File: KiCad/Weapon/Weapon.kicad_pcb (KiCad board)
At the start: 2 copper layers, 97.3 x 74.4 mm, 33 parts, among them IC1 ATMEGA328-P, J1 MICRO_USB, P1 2P_CGRID_M, P2 USB-TTL, P3 2P_CGRID_M, Q1 NPN, Q2 NPN, U1 MCP73831, U2 RFID-RC522, U3 LM1084IT-3.3/NOPB, X1 16MHz

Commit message: Quick Update #1 4/28
Added resistor (220) to buzzer in weapon sch,net,pcb
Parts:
- added R7: 220, R4, F.Cu at (53.9, 77.1)
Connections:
- LS1 pad 1: N-0000013 -> N-0000014
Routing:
- net N-0000013: track 15.8 -> 3.79 mm
- net N-0000014: track 0.00 -> 10.2 mm

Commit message: Quick Update #2 4/28
Changes to Weapon PCB
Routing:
- net GND: track 55.6 -> 2.55 mm
- net +3.3V: track 32.7 -> 0.00 mm
- net N-000001: track 14.2 -> 10.9 mm
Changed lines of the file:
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@@
     (links 66)
     (no_connects 0)
-    (area 32.207999 17.082299 129.590001 91.629701)
+    (area 32.002999 17.082299 129.590001 91.629701)
     (thickness 1.6)
     (drawings 28)
-    (tracks 177)
+    (tracks 168)
     (zones 0)
     (modules 34)
@@
   (gr_line (start 32.258 60.452) (end 70.358 60.452) (angle 90) (layer F.SilkS) (width 0.2))
   (gr_line (start 32.258 35.052) (end 32.258 60.452) (angle 90) (layer F.SilkS) (width 0.2))
-  (segment (start 87.4776 47.4218) (end 97.536 47.4218) (width 0.508) (layer B.Cu) (net 1))
-  (segment (start 100.3808 44.577) (end 100.3808 25.92832) (width 0.508) (layer B.Cu) (net 1))
-  (segment (start 97.536 47.4218) (end 100.3808 44.577) (width 0.508) (layer B.Cu) (net 1))
-  (segment (start 85.344 43.942) (end 87.44712 43.942) (width 0.508) (layer F.Cu) (net 2))
-  (segment (start 87.44712 43.942) (end 92.75826 38.63086) (width 0.508) (layer F.Cu) (net 2))
-  (segment (start 92.75826 38.63086) (end 105.4608 25.92832) (width 0.508) (layer F.Cu) (net 2))
-  (segment (start 87.44712 43.942) (end 105.4608 25.92832) (width 0.254) (layer F.Cu) (net 2))
   (segment (start 37.807 67.198) (end 39.6644 67.198) (width 0.391) (layer F.Cu) (net 2))
   (segment (start 39.6644 67.198) (end 40.1574 67.691) (width 0.391) (layer F.Cu) (net 2))
@@
   (segment (start 73.7235 80.137) (end 73.7235 79.9465) (width 0.254) (layer B.Cu) (net 4))
   (segment (start 73.7235 79.9465) (end 77.216 76.454) (width 0.254) (layer B.Cu) (net 4))
-  (segment (start 36.068 33.147) (end 36.068 27.432) (width 0.254) (layer B.Cu) (net 5))
-  (segment (start 36.322 27.178) (end 44.45 27.178) (width 0.254) (layer B.Cu) (net 5))
-  (segment (start 36.068 27.432) (end 36.322 27.178) (width 0.254) (layer B.Cu) (net 5))
+  (segment (start 44.45 27.178) (end 42.037 27.178) (width 0.508) (layer B.Cu) (net 5))
+  (segment (start 42.037 27.178) (end 36.068 33.147) (width 0.508) (layer B.Cu) (net 5))
   (segment (start 63.5635 80.137) (end 59.8805 80.137) (width 0.254) (layer B.Cu) (net 6))
   (segment (start 59.8805 80.137) (end 59.563 80.4545) (width 0.254) (layer B.Cu) (net 6))
-  (segment (start 57.023 80.4545) (end 55.6895 80.4545) (width 0.508) (layer B.Cu) (net 7) (status 400000))
-  (segment (start 55.6895 80.4545) (end 53.9496 82.1944) (width 0.508) (layer B.Cu) (net 7) (status 800000))
-  (segment (start 53.9496 72.0344) (end 56.5631 72.0344) (width 0.508) (layer B.Cu) (net 8) (status 400000))
-  (segment (start 56.5631 72.0344) (end 61.9125 66.685) (width 0.508) (layer B.Cu) (net 8) (status 800000))
+  (segment (start 57.023 80.4545) (end 55.6895 80.4545) (width 0.508) (layer B.Cu) (net 7))
+  (segment (start 55.6895 80.4545) (end 53.9496 82.1944) (width 0.508) (layer B.Cu) (net 7))
+  (segment (start 53.9496 72.0344) (end 56.5631 72.0344) (width 0.508) (layer B.Cu) (net 8))
+  (segment (start 56.5631 72.0344) (end 61.9125 66.685) (width 0.508) (layer B.Cu) (net 8))
   (segment (start 52.705 66.294) (end 52.705 64.262) (width 0.254) (layer B.Cu) (net 9))
   (segment (start 52.705 64.262) (end 54.864 62.103) (width 0.254) (layer B.Cu) (net 9))
@@
   (segment (start 71.882 50.038) (end 71.882 52.578) (width 0.254) (layer F.Cu) (net 26))
   (via (at 71.882 50.038) (size 0.889) (layers F.Cu B.Cu) (net 26))
+  (segment (start 45.0215 32.7152) (end 45.0215 31.7373) (width 0.508) (layer B.Cu) (net 27))
+  (segment (start 45.0215 31.7373) (end 47.2948 29.464) (width 0.508) (layer B.Cu) (net 27))
   (segment (start 71.5264 43.307) (end 68.6054 40.386) (width 0.508) (layer F.Cu) (net 27))
   (segment (start 73.533 43.307) (end 71.5264 43.307) (width 0.508) (layer F.Cu) (net 27))
@@
   (segment (start 82.042 40.894) (end 82.042 42.164) (width 0.508) (layer B.Cu) (net 27))
   (segment (start 82.042 42.164) (end 80.264 43.942) (width 0.508) (layer B.Cu) (net 27))
-  (segment (start 46.6725 29.464) (end 49.403 29.464) (width 0.508) (layer B.Cu) (net 27))
-  (segment (start 46.6725 29.464) (end 46.609 29.464) (width 0.254) (layer B.Cu) (net 27))
-  (segment (start 46.609 29.464) (end 46.609 31.496) (width 0.508) (layer B.Cu) (net 27))
-  (segment (start 46.609 31.496) (end 46.482 31.623) (width 0.254) (layer B.Cu) (net 27))
-  (segment (start 46.482 31.623) (end 45.0215 31.623) (width 0.508) (layer B.Cu) (net 27))
-  (segment (start 45.0215 31.623) (end 45.0215 37.0967) (width 0.508) (layer B.Cu) (net 27))
+  (segment (start 47.2948 29.464) (end 49.403 29.464) (width 0.508) (layer B.Cu) (net 27))
+  (segment (start 45.0215 31.623) (end 45.0215 32.7152) (width 0.508) (layer B.Cu) (net 27))
+  (segment (start 45.0215 32.7152) (end 45.0215 37.0967) (width 0.508) (layer B.Cu) (net 27))
   (segment (start 51.181 74.295) (end 54.8005 77.9145) (width 0.508) (layer F.Cu) (net 27))
   (segment (start 40.132 31.623) (end 38.608 33.147) (width 0.508) (layer B.Cu) (net 27))
@@
     (polygon
       (pts
-        (xy 89.4588 85.8647) (xy 32.258 85.8647) (xy 32.258 22.8473) (xy 89.4588 22.8473)
+        (xy 106.807 28.9941) (xy 89.4588 28.9941) (xy 89.4588 85.8647) (xy 32.258 85.8647) (xy 32.258 22.8473)
+        (xy 106.807 22.8473)
       )
     )
@@
     (polygon
       (pts
-        (xy 89.4588 85.8647) (xy 32.258 85.8647) (xy 32.258 22.8473) (xy 89.4588 22.8473)
+        (xy 106.807 28.9941) (xy 89.4588 28.9941) (xy 89.4588 85.8647) (xy 32.258 85.8647) (xy 32.258 22.8473)
+        (xy 89.4588 22.8473) (xy 106.807 22.8473) (xy 106.807 28.9941)
       )
     )

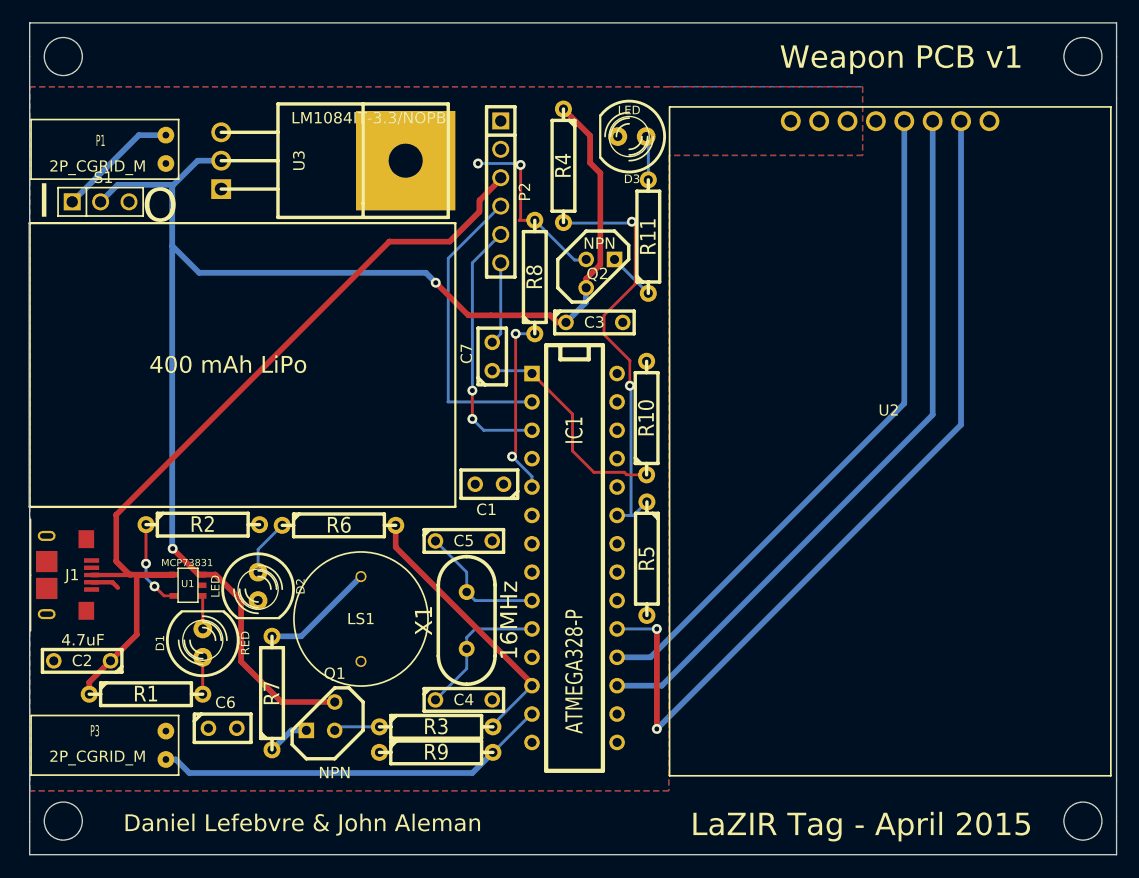
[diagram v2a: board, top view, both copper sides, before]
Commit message: Quick Update #3 4/28
Refinement of text placement
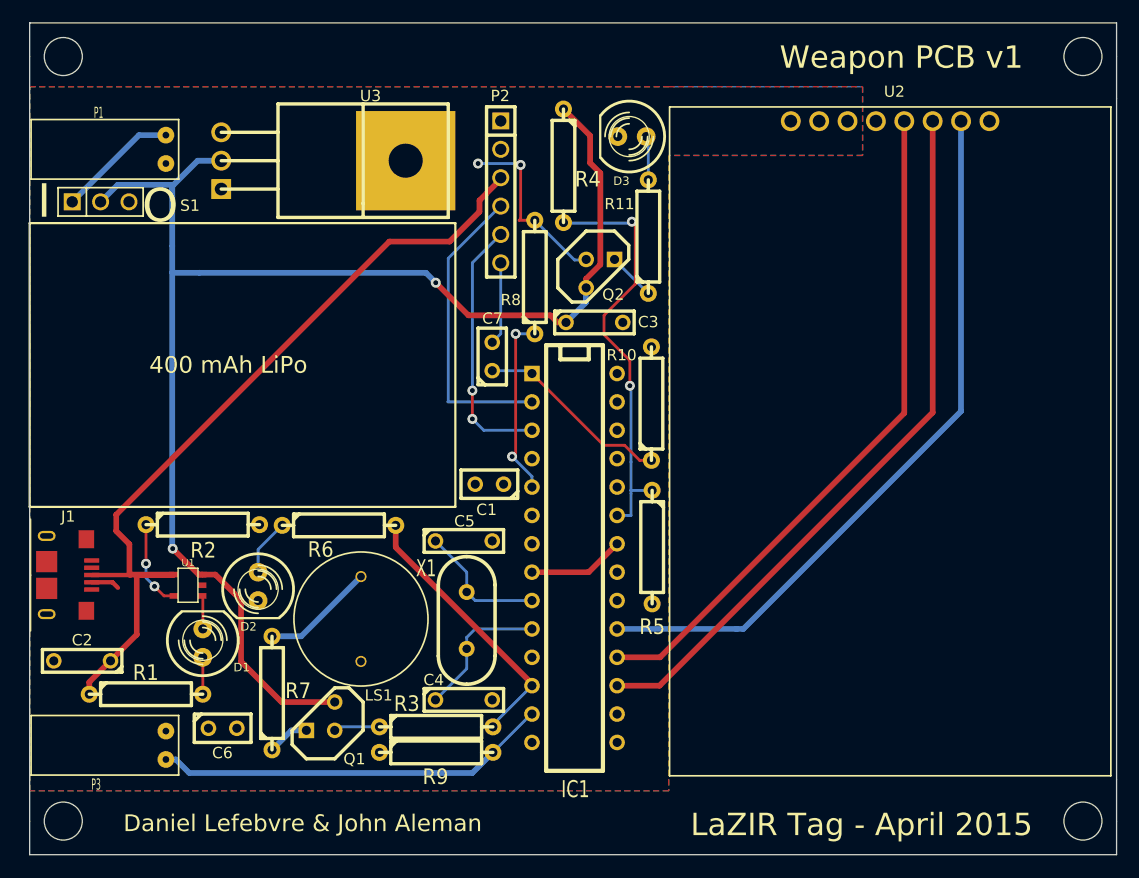
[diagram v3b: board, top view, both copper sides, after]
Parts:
- moved R10 1.37 mm to (87.9, 51.2)
- moved R5 1.14 mm to (88.0, 64.0)
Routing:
- net RFID-SCK: track 78.4 -> 64.8 mm, vias 2 -> 0
- net GND: track 2.55 -> 11.2 mm
- net Reset: track 19.6 -> 17.6 mm
- net V-Bat: track 129.1 -> 128.1 mm
